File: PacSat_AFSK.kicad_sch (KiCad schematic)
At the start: 4 parts

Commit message: More hacking on things
Signed-off-by: Corey Minyard <corey@minyard.net>
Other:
- removed sheet SPI_CTL
- note removed: "800"
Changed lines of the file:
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@@
-		)
-	)
-	(text "800"
-		(exclude_from_sim no)
-		(at 271.78 88.9 0)
-		(effects
-			(font
-				(size 1.524 1.524)
-			)
-			(justify left bottom)
 		)
 	)
@@
 				)
 			)
-		)
-	)
-	(sheet
-		(at 270.51 74.93)
-		(size 52.07 15.24)
-		(exclude_from_sim no)
-		(in_bom yes)
-		(on_board yes)
-		(dnp no)
-		(fields_autoplaced yes)
-		(stroke
-			(width 0)
-			(type solid)
-		)
-		(fill
-			(color 0 0 0 0.0000)
-		)
-		(property "Sheetname" "SPI_CTL"
-			(at 270.51 74.0914 0)
-			(effects
-				(font
-					(size 1.524 1.524)
-				)
-				(justify left bottom)
-			)
-		)
-		(property "Sheetfile" "SPI_CTL.kicad_sch"
-			(at 270.51 90.8562 0)
-			(effects
-				(font
-					(size 1.524 1.524)
-				)
-				(justify left top)
-			)
-		)
-		(instances
-			(project "PacSat_AFSK"
-				(path "/cc9f42d2-6985-41ac-acab-5ab7b01c5b38"
-					(page "10")
-				)
-			)

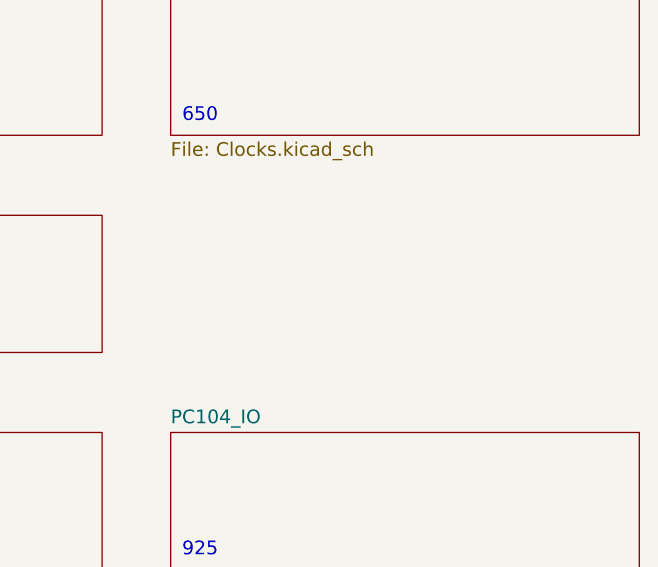
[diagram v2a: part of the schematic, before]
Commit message: Add a CPU thermsistor
Signed-off-by: Corey Minyard <corey@minyard.net>
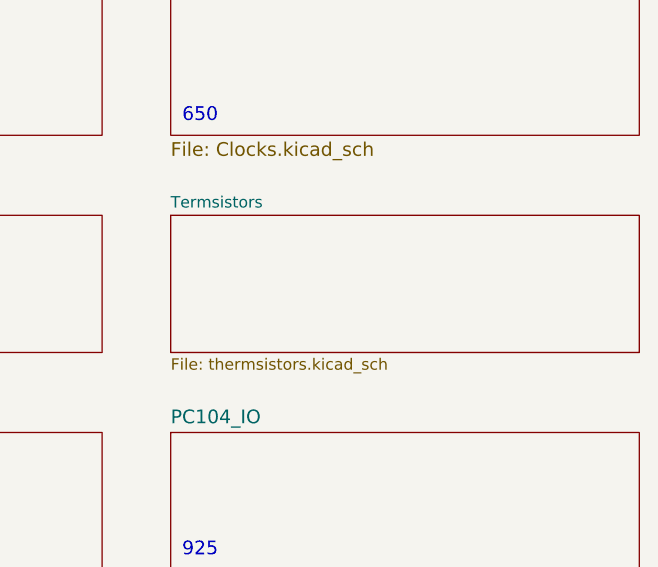
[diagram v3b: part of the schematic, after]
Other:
- added sheet Termsistors (thermsistors.kicad_sch)
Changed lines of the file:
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@@
+	)
+	(sheet
+		(at 270.51 74.93)
+		(size 52.07 15.24)
+		(exclude_from_sim no)
+		(in_bom yes)
+		(on_board yes)
+		(dnp no)
+		(fields_autoplaced yes)
+		(stroke
+			(width 0.1524)
+			(type solid)
+		)
+		(fill
+			(color 0 0 0 0.0000)
+		)
+		(property "Sheetname" "Termsistors"
+			(at 270.51 74.2184 0)
+			(effects
+				(font
+					(size 1.27 1.27)
+				)
+				(justify left bottom)
+			)
+		)
+		(property "Sheetfile" "thermsistors.kicad_sch"
+			(at 270.51 90.7546 0)
+			(effects
+				(font
+					(size 1.27 1.27)
+				)
+				(justify left top)
+			)
+		)
+		(instances
+			(project "PacSat_AFSK"
+				(path "/cc9f42d2-6985-41ac-acab-5ab7b01c5b38"
+					(page "15")
+				)
+			)
+		)
 	)
 	(sheet

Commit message: Finished up the TX PA section.
Signed-off-by: Corey Minyard <corey@minyard.net>
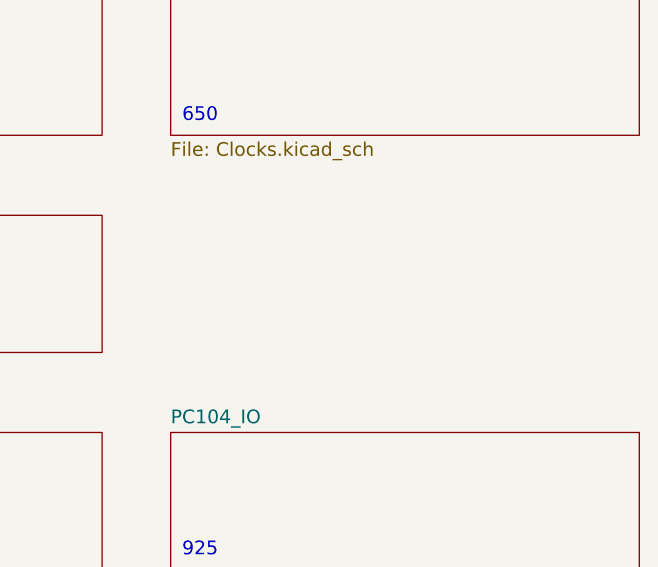
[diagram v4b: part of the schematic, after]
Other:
- removed sheet Termsistors
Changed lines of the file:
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@@
-	)
-	(sheet
-		(at 270.51 74.93)
-		(size 52.07 15.24)
-		(exclude_from_sim no)
-		(in_bom yes)
-		(on_board yes)
-		(dnp no)
-		(fields_autoplaced yes)
-		(stroke
-			(width 0.1524)
-			(type solid)
-		)
-		(fill
-			(color 0 0 0 0.0000)
-		)
-		(property "Sheetname" "Termsistors"
-			(at 270.51 74.2184 0)
-			(effects
-				(font
-					(size 1.27 1.27)
-				)
-				(justify left bottom)
-			)
-		)
-		(property "Sheetfile" "thermsistors.kicad_sch"
-			(at 270.51 90.7546 0)
-			(effects
-				(font
-					(size 1.27 1.27)
-				)
-				(justify left top)
-			)
-		)
-		(instances
-			(project "PacSat_AFSK"
-				(path "/cc9f42d2-6985-41ac-acab-5ab7b01c5b38"
-					(page "15")
-				)
-			)
-		)
 	)
 	(sheet

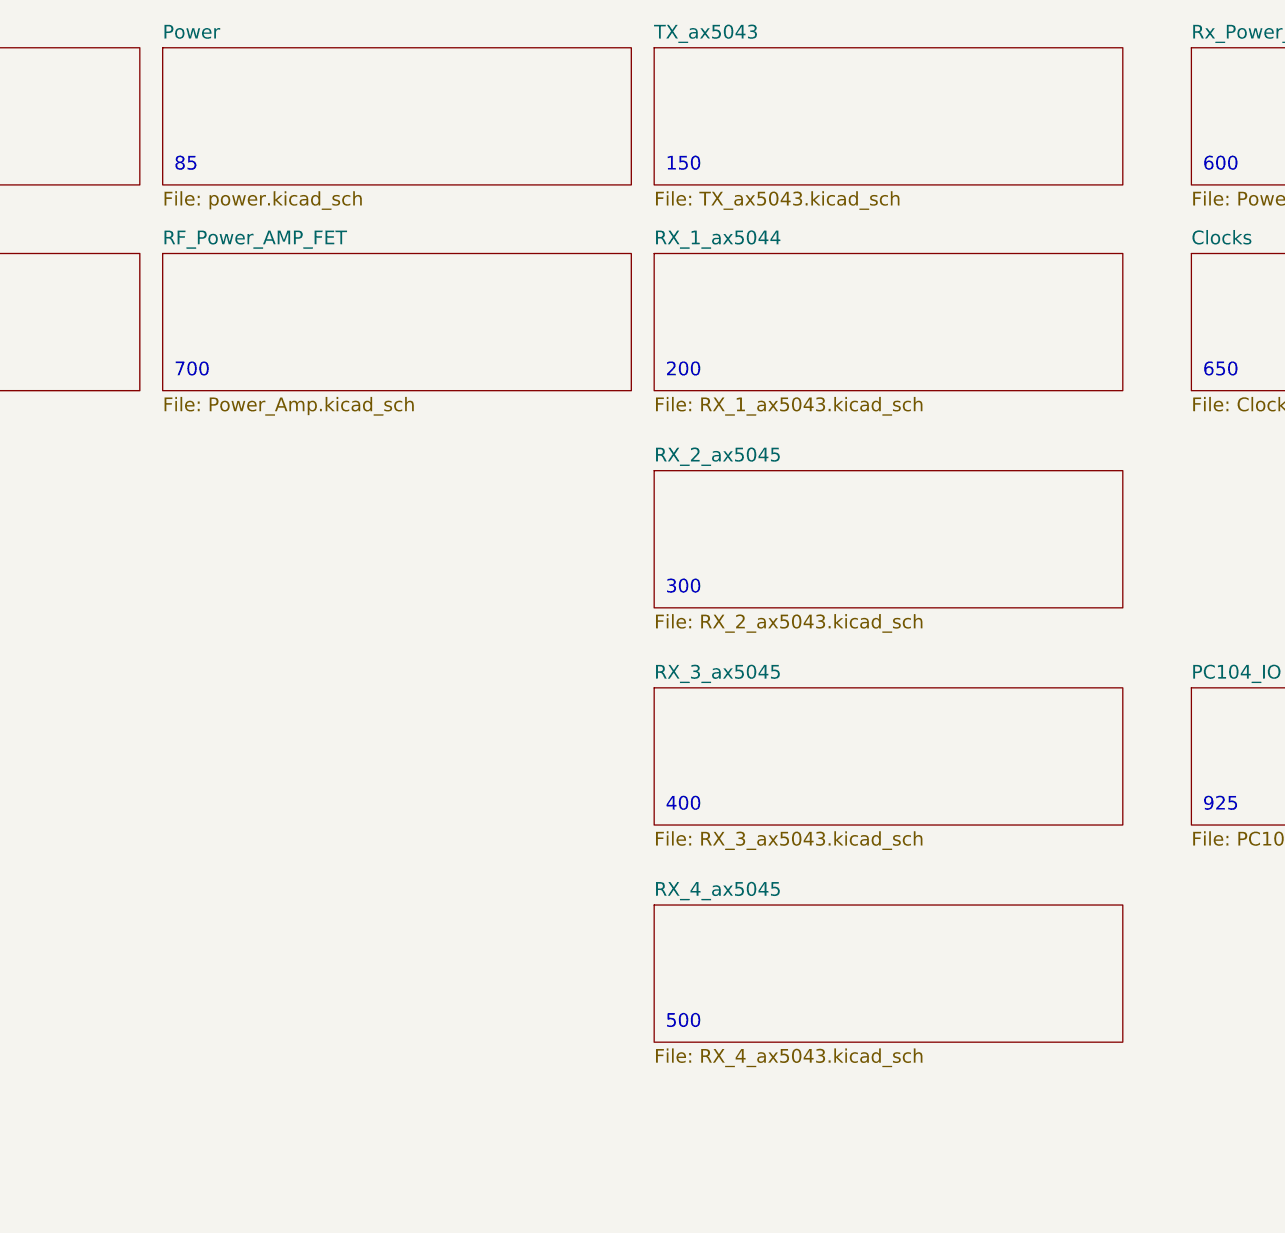
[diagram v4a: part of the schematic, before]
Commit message: Create hierarchical sheets for the AX5043s
Signed-off-by: Corey Minyard <corey@minyard.net>
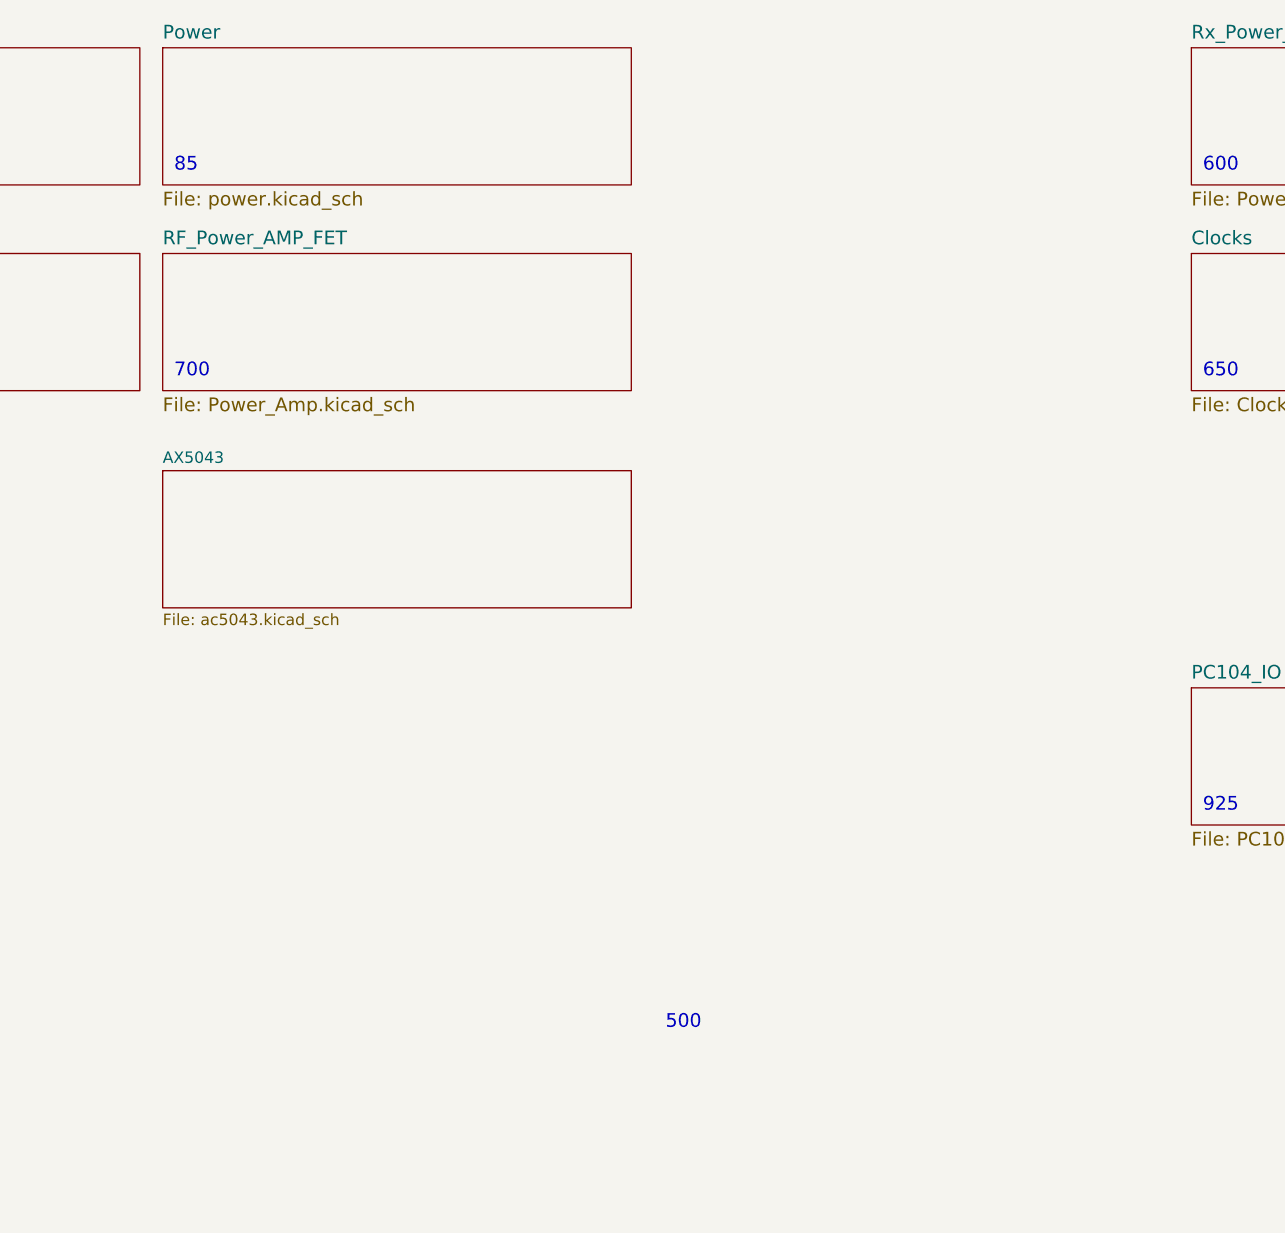
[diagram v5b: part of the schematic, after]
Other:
- removed sheet RX_1_ax5044
- removed sheet RX_2_ax5045
- removed sheet RX_3_ax5045
- removed sheet RX_4_ax5045
- removed sheet TX_ax5043
- added sheet AX5043 (ac5043.kicad_sch)
- note removed: "150"
- note removed: "200"
- note removed: "300"
- note removed: "400"
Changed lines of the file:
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@@
-		)
-	)
-	(text "200"
-		(exclude_from_sim no)
-		(at 212.09 64.77 0)
-		(effects
-			(font
-				(size 1.524 1.524)
-			)
-			(justify left bottom)
-		)
-	)
-	(text "400"
-		(exclude_from_sim no)
-		(at 212.09 113.03 0)
-		(effects
-			(font
-				(size 1.524 1.524)
-			)
-			(justify left bottom)
 		)
 	)
@@
 		)
 	)
-	(text "150"
-		(exclude_from_sim no)
-		(at 212.09 41.91 0)
-		(effects
-			(font
-				(size 1.524 1.524)
-			)
-			(justify left bottom)
-		)
-	)
 	(text "75"
 		(exclude_from_sim no)
@@
 		)
 	)
-	(text "300"
-		(exclude_from_sim no)
-		(at 212.09 88.9 0)
-		(effects
-			(font
-				(size 1.524 1.524)
-			)
-			(justify left bottom)
-		)
-	)
 	(text "700"
 		(exclude_from_sim no)
@@
 	)
 	(sheet
-		(at 210.82 27.94)
+		(at 156.21 27.94)
 		(size 52.07 15.24)
 		(exclude_from_sim no)
@@
 			(color 0 0 0 0.0000)
 		)
-		(property "Sheetname" "TX_ax5043"
-			(at 210.82 27.1014 0)
-			(effects
-				(font
-					(size 1.524 1.524)
-				)
-				(justify left bottom)
-			)
-		)
-		(property "Sheetfile" "TX_ax5043.kicad_sch"
-			(at 210.82 43.8662 0)
-			(effects
-				(font
-					(size 1.524 1.524)
-				)
-				(justify left top)
-			)
-		)
-		(instances
-			(project "PacSat_AFSK"
-				(path "/cc9f42d2-6985-41ac-acab-5ab7b01c5b38"
-					(page "6")
-				)
-			)
-		)
-	)
-	(sheet
-		(at 156.21 27.94)
-		(size 52.07 15.24)
-		(exclude_from_sim no)
-		(in_bom yes)
-		(on_board yes)
-		(dnp no)
-		(fields_autoplaced yes)
-		(stroke
-			(width 0)
-			(type solid)
-		)
-		(fill
-			(color 0 0 0 0.0000)
-		)
 		(property "Sheetname" "Power"
 			(at 156.21 27.1014 0)
@@
 				(path "/cc9f42d2-6985-41ac-acab-5ab7b01c5b38"
 					(page "8")
-				)
-			)
-		)
-	)
-	(sheet
-		(at 210.82 50.8)
-		(size 52.07 15.24)
-		(exclude_from_sim no)
-		(in_bom yes)
-		(on_board yes)
-		(dnp no)
-		(fields_autoplaced yes)
-		(stroke
-			(width 0)
-			(type solid)
-		)
-		(fill
-			(color 0 0 0 0.0000)
-		)
-		(property "Sheetname" "RX_1_ax5044"
-			(at 210.82 49.9614 0)
-			(effects
-				(font
-					(size 1.524 1.524)
-				)
-				(justify left bottom)
-			)
-		)
-		(property "Sheetfile" "RX_1_ax5043.kicad_sch"
-			(at 210.82 66.7262 0)
-			(effects
-				(font
-					(size 1.524 1.524)
-				)
-				(justify left top)
-			)
-		)
-		(instances
-			(project "PacSat_AFSK"
-				(path "/cc9f42d2-6985-41ac-acab-5ab7b01c5b38"
-					(page "5")
 				)
 			)
@@
 	)
 	(sheet
-		(at 210.82 74.93)
+		(at 101.6 50.8)
 		(size 52.07 15.24)
 		(exclude_from_sim no)
@@
 		(fields_autoplaced yes)
 		(stroke
-			(width 0)
+			(width 0.1524)
 			(type solid)
 		)
@@
 			(color 0 0 0 0.0000)
 		)
-		(property "Sheetname" "RX_2_ax5045"
-			(at 210.82 74.0914 0)
-			(effects
-				(font
-					(size 1.524 1.524)
-				)
-				(justify left bottom)
-			)
-		)
-		(property "Sheetfile" "RX_2_ax5043.kicad_sch"
-			(at 210.82 90.8562 0)
-			(effects
-				(font
-					(size 1.524 1.524)
-				)
-				(justify left top)
-			)
-		)
-		(instances
-			(project "PacSat_AFSK"
-				(path "/cc9f42d2-6985-41ac-acab-5ab7b01c5b38"
-					(page "7")
-				)
-			)
-		)
-	)
-	(sheet
-		(at 101.6 50.8)
-		(size 52.07 15.24)
-		(exclude_from_sim no)
-		(in_bom yes)
-		(on_board yes)
-		(dnp no)
-		(fields_autoplaced yes)
-		(stroke
-			(width 0.1524)
-			(type solid)
-		)
-		(fill
-			(color 0 0 0 0.0000)
-		)
 		(property "Sheetname" "Memory"
 			(at 101.6 50.0884 0)
@@
 				(path "/cc9f42d2-6985-41ac-acab-5ab7b01c5b38"
 					(page "17")
-				)
-			)
-		)
-	)
-	(sheet
-		(at 210.82 99.06)
-		(size 52.07 15.24)
-		(exclude_from_sim no)
-		(in_bom yes)
-		(on_board yes)
-		(dnp no)
-		(fields_autoplaced yes)
-		(stroke
-			(width 0)
-			(type solid)
-		)
-		(fill
-			(color 0 0 0 0.0000)
-		)
-		(property "Sheetname" "RX_3_ax5045"
-			(at 210.82 98.2214 0)
-			(effects
-				(font
-					(size 1.524 1.524)
-				)
-				(justify left bottom)
-			)
-		)
-		(property "Sheetfile" "RX_3_ax5043.kicad_sch"
-			(at 210.82 114.9862 0)
-			(effects
-				(font
-					(size 1.524 1.524)
-				)
-				(justify left top)
-			)
-		)
-		(instances
-			(project "PacSat_AFSK"
-				(path "/cc9f42d2-6985-41ac-acab-5ab7b01c5b38"
-					(page "9")
 				)
 			)
@@
 	)
 	(sheet
-		(at 210.82 123.19)
+		(at 156.21 74.93)
 		(size 52.07 15.24)
 		(exclude_from_sim no)
@@
 		(fields_autoplaced yes)
 		(stroke
-			(width 0)
+			(width 0.1524)
 			(type solid)
 		)
@@
 			(color 0 0 0 0.0000)
 		)
-		(property "Sheetname" "RX_4_ax5045"
-			(at 210.82 122.3514 0)
-			(effects
-				(font
-					(size 1.524 1.524)
+		(property "Sheetname" "AX5043"
+			(at 156.21 74.2184 0)
+			(effects
+				(font
+					(size 1.27 1.27)
 				)
 				(justify left bottom)
 			)
 		)
-		(property "Sheetfile" "RX_4_ax5043.kicad_sch"
-			(at 210.82 139.1162 0)
-			(effects
-				(font
-					(size 1.524 1.524)
+		(property "Sheetfile" "ac5043.kicad_sch"
+			(at 156.21 90.7546 0)
+			(effects
+				(font
+					(size 1.27 1.27)
 				)
 				(justify left top)
@@
 			(project "PacSat_AFSK"
 				(path "/cc9f42d2-6985-41ac-acab-5ab7b01c5b38"
-					(page "11")
-				)
-			)
+					(page "15")
+				)
+			)
